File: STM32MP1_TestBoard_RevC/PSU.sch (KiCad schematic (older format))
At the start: 35 parts, among them J11 USB_C_Receptacle_USB2.0, J9 Barrel_Jack, U3 SE8233X2, U4 TPS563200DDCT, U5 SiP3250x, U6 SiP3250x

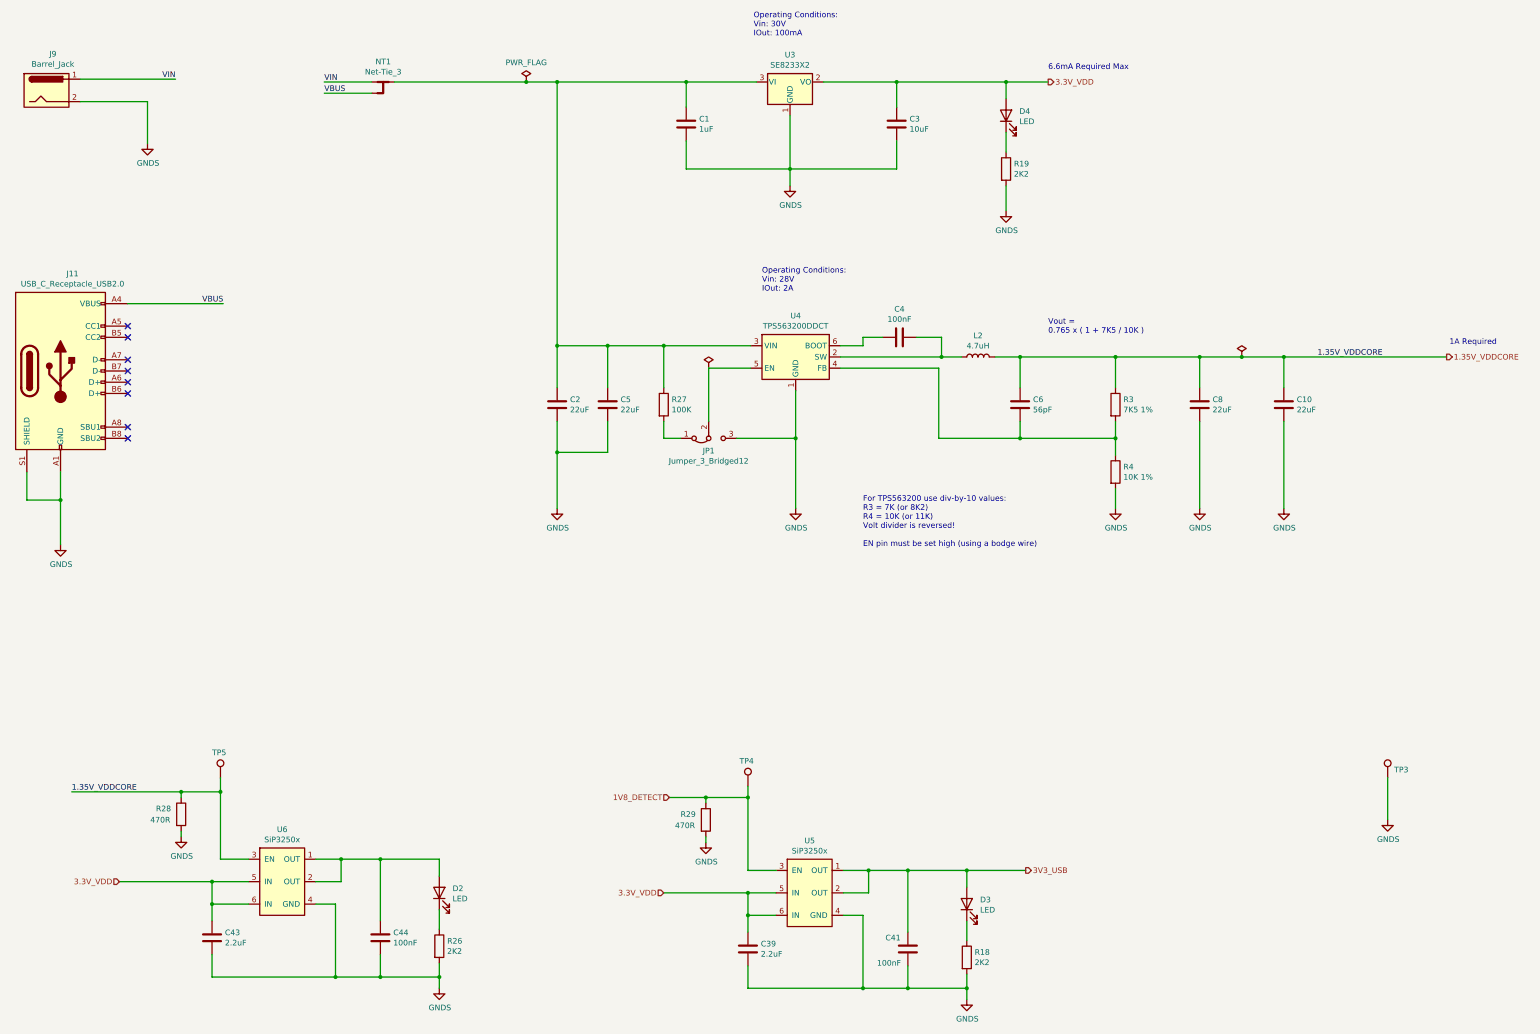
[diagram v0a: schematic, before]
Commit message: HW changes
- Changed buck converter(TPS42402) to LDO (AZ1117)
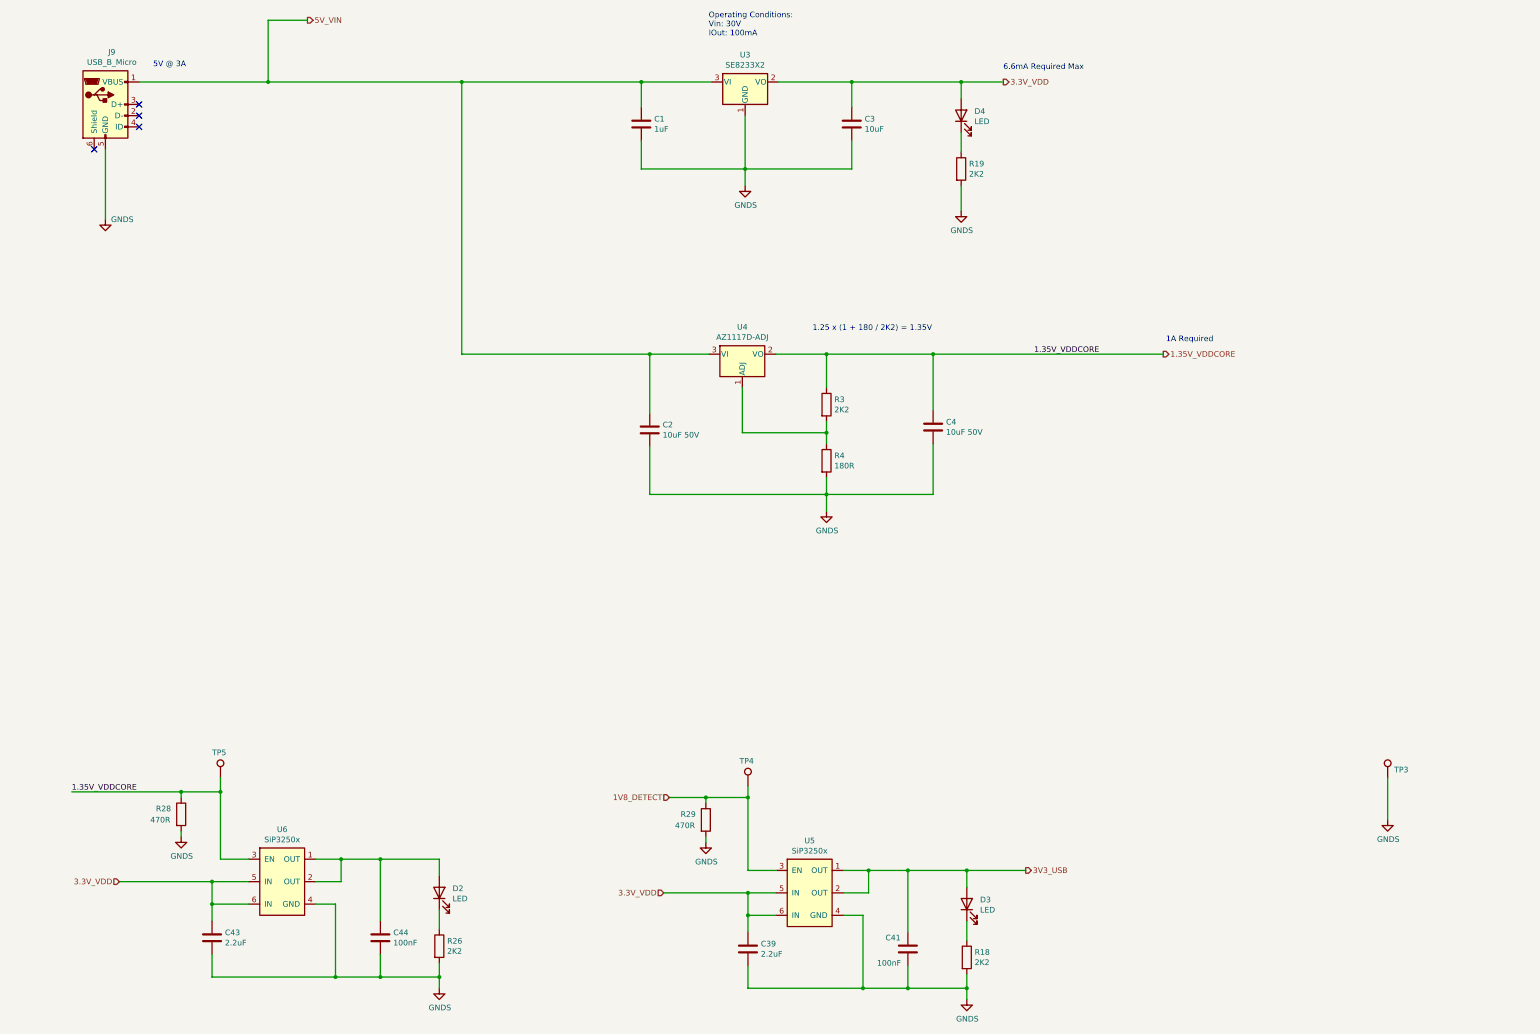
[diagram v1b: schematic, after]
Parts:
- removed C10, C5, C8: 22uF, Capacitor_SMD:C_1206_3216Metric_Pad1.33x1.80mm_HandSolder, symbol Device:C
- removed C6: 56pF, Capacitor_SMD:C_0402_1005Metric_Pad0.74x0.62mm_HandSolder, symbol Device:C
- removed J11: USB_C_Receptacle_USB2.0, MolexUSB_TypeC:213716-0001_THT_Socket_RightAngle, symbol Connector:USB_C_Receptacle_USB2.0
- removed J9: Barrel_Jack, Connector_BarrelJack:BarrelJack_Horizontal, symbol Connector:Barrel_Jack
- removed JP1: Jumper_3_Bridged12, Jumper:SolderJumper-3_P1.3mm_Bridged12_RoundedPad1.0x1.5mm, symbol Jumper:Jumper_3_Bridged12
- removed L2: 4.7uH, Inductor_SMD:L_Bourns-SRN6028, symbol Device:L
- removed NT1: Net-Tie_3, NetTie:NetTie-3_SMD_Pad0.5mm, symbol Device:Net-Tie_3
- removed R27: 100K, Resistor_SMD:R_0805_2012Metric_Pad1.20x1.40mm_HandSolder, symbol Device:R
- removed U4: TPS563200DDCT, Package_TO_SOT_SMD:SOT-23-6, symbol Regulator_Switching:TPS54202DDC
- added J9: USB_B_Micro, Connector_USB:USB_Micro-B_Molex-105017-0001, symbol Connector:USB_B_Micro
- added U4: AZ1117D-ADJ, Package_TO_SOT_SMD:TO-252-2, symbol Regulator_Linear:AZ1117D-ADJ
- C2: value 22uF -> 10uF 50V
- C4: value 100nF -> 10uF 50V; footprint Capacitor_SMD:C_0402_1005Metric_Pad0.74x0.62mm_HandSolder -> Capacitor_SMD:C_1206_3216Metric_Pad1.33x1.80mm_HandSolder; LCSC C1525 -> (none); Mfr (none) -> Kemet; PartNo (none) -> C1206C226M8PACTU
- R3: value 7K5 1% -> 2K2; LCSC C25741 -> C25879
- R4: value 10K 1% -> 180R; LCSC C1542 -> C25879
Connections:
- net 1.35V_VDDCORE: now also C4.1, U4.2 (VO)
- net GNDS: now also C4.2, J9.5 (GND)
- net 5V_VIN: now reaches C1.1, C2.1, U3.3 (VI)
- net 5V_VIN: now also J9.1 (VBUS), U4.3 (VI)
- net at R3.2, R4.1: now also U4.1 (ADJ)
- no-connect marks 8 -> 4
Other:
- note added: "1.25 x (1 + 180 / 2K2) = 1.35V"
- note added: "5V @ 3A"
- note removed: "For TPS563200 use div-by-10 values:\nR3 = 7K (or 8K2)\nR4 = 10K (or 11K)\nVolt divider is reversed!\n\nEN pin must be set high (using a bodge wire)"
- note removed: "Operating Conditions:\nVin: 28V\nIOut: 2A"
- note removed: "Vout = \n0.765 x ( 1 + 7K5 / 10K )"
- moved on the sheet: C1, C3, D4, R19, U3
